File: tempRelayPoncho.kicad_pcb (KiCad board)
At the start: 2 copper layers, 36 parts, among them J1 Screw_Terminal_1x02, J2 Screw_Terminal_1x02, J3 Screw_Terminal_1x02, J4 Screw_Terminal_1x02, J5 Screw_Terminal_1x02, J6 Screw_Terminal_1x02, Q1 MMBT3904, Q2 MMBT3904, U1 NUP2105LT1G, U2 MAX31855KASA+, U3 MCP601R, U4 G5LE-1A-5DC, U6 G5LE-1A-5DC

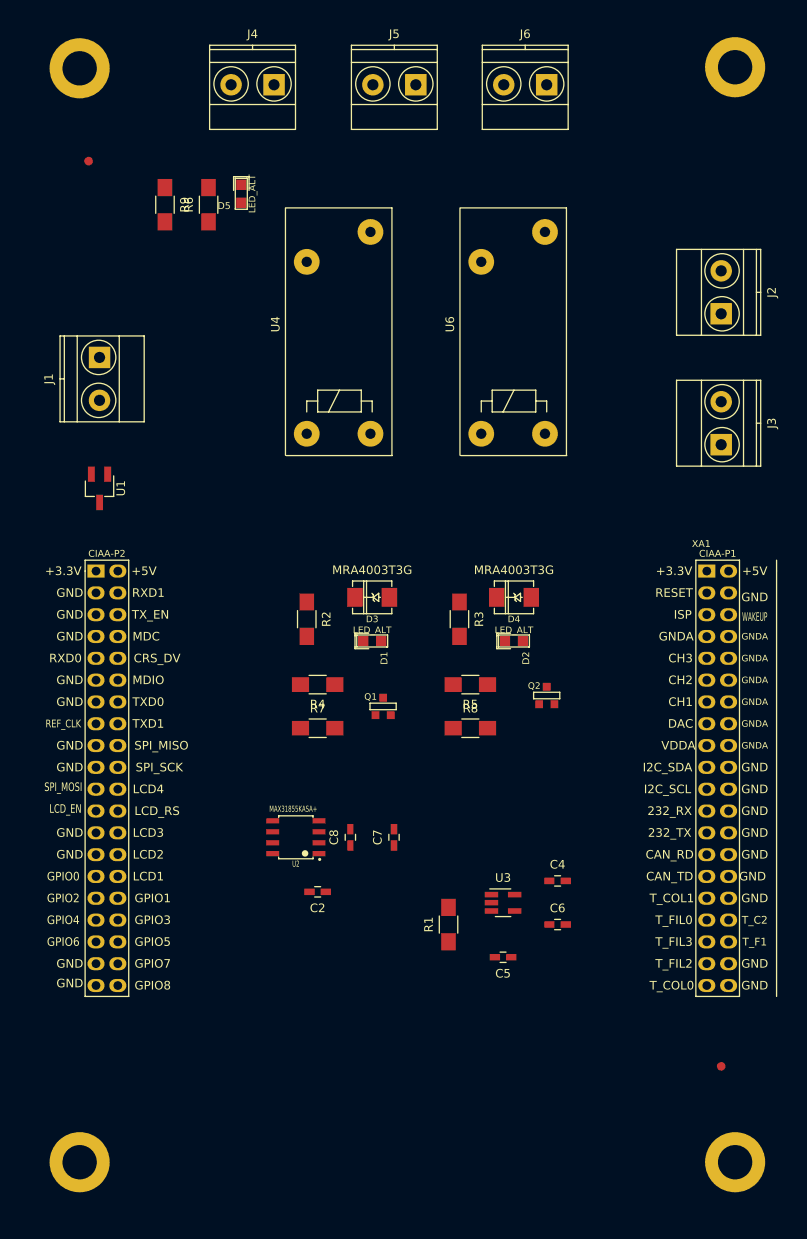
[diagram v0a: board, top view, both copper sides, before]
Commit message: Primer version del PCB
Se agregan modificaciones segun primer correccion. Se carga primer version  del PCB.
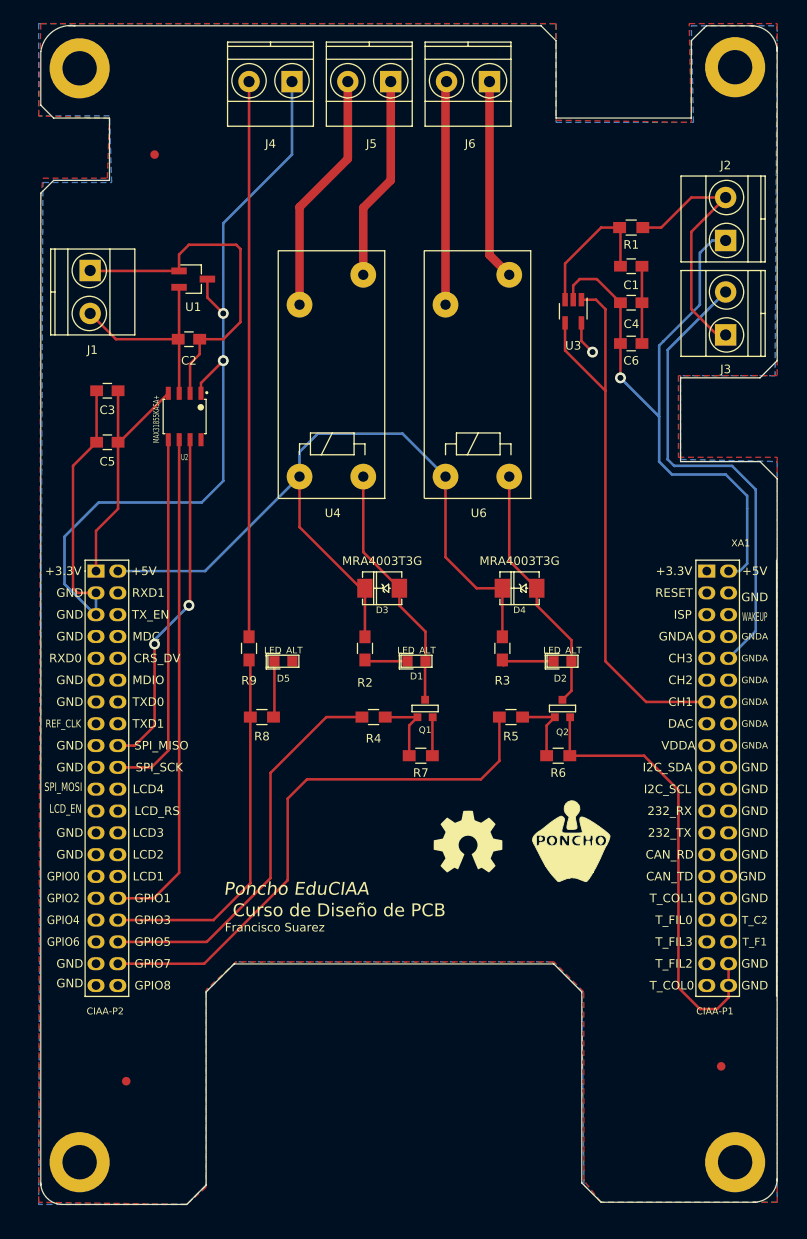
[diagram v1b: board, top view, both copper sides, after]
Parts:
- removed C7: 10u, footprints:C_0603_HandSoldering
- removed C8: 100n, footprints:C_0603_HandSoldering
- added C1: 10u, footprints:C_0805_HandSoldering, F.Cu at (147.0, 60.5)
- added C3: 10u, footprints:C_0805_HandSoldering, F.Cu at (86.0, 75.0)
- added F3: FIDUCIAL, footprints:Fiducial_1mm, F.Cu at (88.2, 155.4)
- added G***: LOGO, footprints:Logo_Poncho, F.Cu at (140.0, 127.5)
- added G101: Logo_OSHWA, footprints:Logo_OSHWA, F.Cu at (128.0, 127.5)
- C2, C4, C6: footprint footprints:C_0603_HandSoldering -> footprints:C_0805_HandSoldering
- C5: value 10u -> 100n; footprint footprints:C_0603_HandSoldering -> footprints:C_0805_HandSoldering
- R1, R2, R3, R4, R5, R7, R9: footprint footprints:R_1206_HandSoldering -> footprints:R_0805_HandSoldering
- R6: value 1k -> 10k; footprint footprints:R_1206_HandSoldering -> footprints:R_0805_HandSoldering
- R8: value 10k -> 1k; footprint footprints:R_1206_HandSoldering -> footprints:R_0805_HandSoldering
- moved R1 83.9 mm to (147.0, 56.0), turned to 0 degrees
- moved R6 76.0 mm to (138.5, 117.5), turned to 180 degrees
- moved C5 75.6 mm to (86.0, 81.0), turned to 0 degrees
- moved U3 69.4 mm to (140.2, 65.8), turned to 270 degrees
- moved C6 68.2 mm to (147.0, 69.5), turned to 180 degrees
- moved C4 67.9 mm to (147.0, 64.8), turned to 180 degrees
- moved C2 66.1 mm to (95.5, 69.0), turned to 0 degrees
- moved D5 54.7 mm to (106.5, 106.5), turned to 180 degrees
- moved R9 52.6 mm to (102.5, 105.0)
- moved U2 50.7 mm to (95.0, 78.0), turned to 270 degrees
- moved U1 26.7 mm to (96.0, 62.0), turned to 0 degrees
- moved R8 24.3 mm to (104.0, 113.0), turned to 180 degrees
- moved J3 12.8 mm to (158.0, 68.5)
- moved R7 12.4 mm to (122.5, 117.5), turned to 180 degrees
- moved J1 10.2 mm to (84.0, 61.0)
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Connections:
- net /conector_ciaa/GNDA renamed GNDA
- C5 pad 2: Net-(C5-Pad2) -> +3V3
- D3 pad 2: +5V -> +5VD
- D4 pad 2: +5V -> +5VD
- R1 pad 1: Net-(C5-Pad2) -> Net-(C1-Pad2)
- R2 pad 1: +5V -> Net-(D1-Pad2)
- R2 pad 2: Net-(D1-Pad2) -> +5VD
- R3 pad 1: +5V -> Net-(D2-Pad2)
- R3 pad 2: Net-(D2-Pad2) -> +5VD
- R4 pad 2: /conector_ciaa/GPIO_2 -> /conector_ciaa/GPIO_5
- R5 pad 2: /conector_ciaa/GPIO_3 -> /conector_ciaa/GPIO_7
- R6 pad 1: /conector_ciaa/GPIO_1 -> GND
- R6 pad 2: Net-(D5-Pad2) -> Net-(Q2-Pad1)
- R8 pad 1: GND -> Net-(D5-Pad2)
- R8 pad 2: Net-(Q2-Pad1) -> /conector_ciaa/GPIO_3
- R9 pad 2: /conector_ciaa/GPIO_1 -> /conector_ciaa/GPIO_3
- U2 pad 4: +3.3V -> +3V3
- U2 pad 6: /conector_ciaa/GPIO_0 -> /conector_ciaa/GPIO_1
- U3 pad 3: Net-(C5-Pad2) -> Net-(C1-Pad2)
- U4 pad 5: +5V -> +5VD
- U6 pad 5: +5V -> +5VD
- XA1 pad 1: +3.3V -> Net-(XA1-Pad1)
- XA1 pad 20: GND -> Net-(XA1-Pad20)
- XA1 pad 22: GND -> Net-(XA1-Pad22)
- XA1 pad 24: GND -> Net-(XA1-Pad24)
- XA1 pad 26: GND -> Net-(XA1-Pad26)
- XA1 pad 28: GND -> Net-(XA1-Pad28)
- XA1 pad 30: GND -> Net-(XA1-Pad30)
- XA1 pad 32: GND -> Net-(XA1-Pad32)
- XA1 pad 41: Net-(XA1-Pad41) -> +3V3
- XA1 pad 42: Net-(XA1-Pad42) -> +5VD
- XA1 pad 47: GND -> Net-(XA1-Pad47)
- XA1 pad 51: GND -> Net-(XA1-Pad51)
- XA1 pad 53: GND -> Net-(XA1-Pad53)
- XA1 pad 57: GND -> Net-(XA1-Pad57)
- XA1 pad 59: GND -> Net-(XA1-Pad59)
- XA1 pad 65: GND -> Net-(XA1-Pad65)
- XA1 pad 67: GND -> Net-(XA1-Pad67)
- XA1 pad 69: /conector_ciaa/GPIO_0 -> Net-(XA1-Pad69)
- XA1 pad 71: /conector_ciaa/GPIO_2 -> Net-(XA1-Pad71)
- XA1 pad 76: Net-(XA1-Pad76) -> /conector_ciaa/GPIO_5
- XA1 pad 77: GND -> Net-(XA1-Pad77)
- XA1 pad 78: Net-(XA1-Pad78) -> /conector_ciaa/GPIO_7
- XA1 pad 79: GND -> Net-(XA1-Pad79)
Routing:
- net GND: track 0.00 -> 193.0 mm, vias 0 -> 3
- net +5VD: track 0.00 -> 94.6 mm
- net +5V: track 0.00 -> 76.1 mm, vias 0 -> 1
- net /conector_ciaa/ADC_1: track 0.00 -> 67.9 mm
- net Net-(J4-Pad2): track 0.00 -> 65.4 mm
- net /conector_ciaa/GPIO_7: track 0.00 -> 64.9 mm
- net /conector_ciaa/GPIO_1: track 0.00 -> 58.9 mm
- net GNDA: track 0.00 -> 55.3 mm
- net /conector_ciaa/GPIO_5: track 0.00 -> 46.4 mm
- net /conector_ciaa/GPIO_3: track 0.00 -> 43.3 mm
- net /inputs_temp/SCK_TCUP: track 0.00 -> 42.9 mm
- net Net-(C2-Pad2): track 0.00 -> 41.0 mm
- net /inputs_temp/MISO_TCUP: track 0.00 -> 40.5 mm, vias 0 -> 2
- net +3V3: track 0.00 -> 31.4 mm
- net Net-(J2-Pad2): track 0.00 -> 31.0 mm
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- added copper zone on B.Cu, net GND
- added copper zone on F.Cu, net GND
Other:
- board outline added: 85.8 x 137.3 mm
- net class Default: trace_width 0.25 -> 0.3; via_dia 0.6 -> 1.27; via_drill 0.4 -> 0.7
- rule trace_min: 0.2 -> 0.3
- rule via_min_drill: 0.3 -> 0.7
- rule via_min_size: 0.4 -> 1.2
- board text added: "Curso de Diseño de PCB"
- board text added: "Francisco Suarez"
- board text added: "Poncho EduCIAA"

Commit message: Correcciones de Revisor
Se agregan algunas de las correcciones del revisor. Las que restan se implementaran luego.
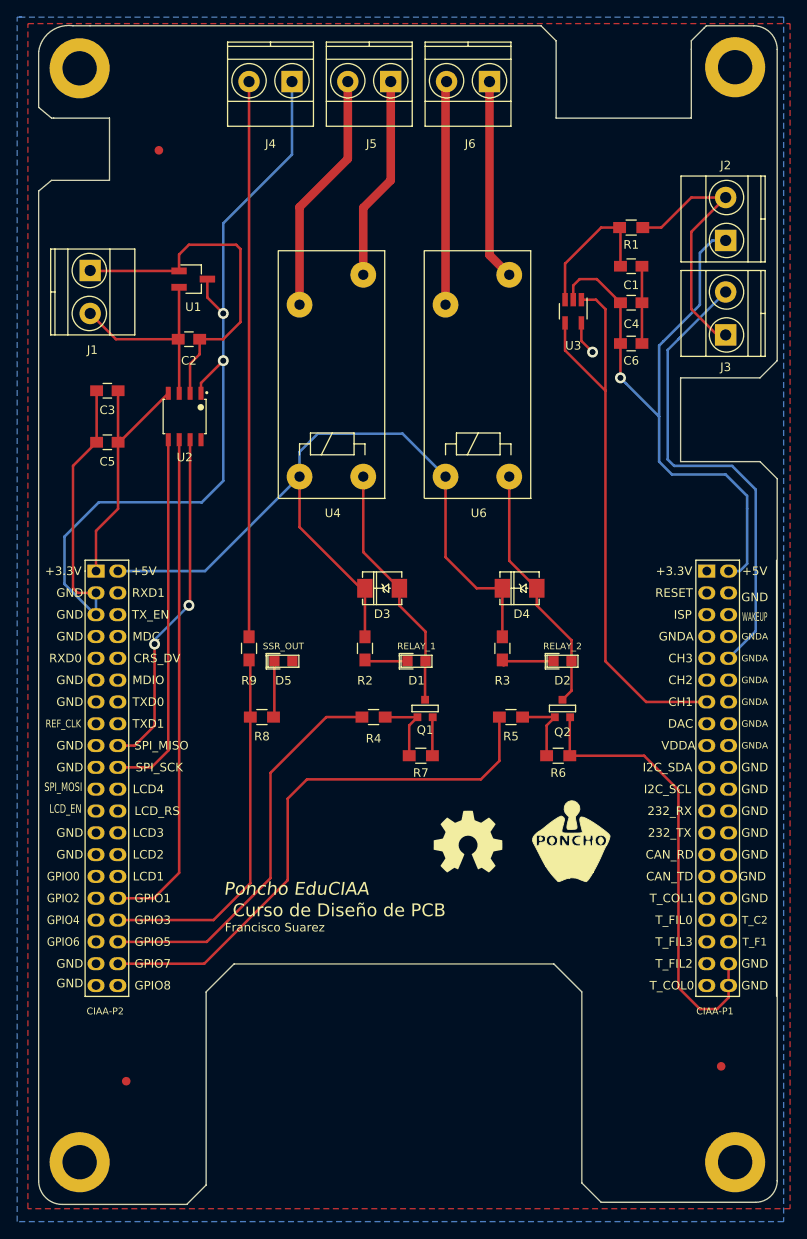
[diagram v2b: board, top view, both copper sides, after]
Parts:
- D1: value LED_ALT -> RELAY_1
- D2: value LED_ALT -> RELAY_2
- D5: value LED_ALT -> SSR_OUT
- moved F1 0.71 mm to (92.0, 47.0)
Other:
- board size 85.8 x 137.3 mm -> 86 x 137.3 mm
- board text added: "Grilla posicionamiento: 1.0 mm Grilla ruteo: 0.25 mm Pista minimo: 0.30 mm Vía minimo: 1.27 mm Agujero minimo: 0.70 mm Capas: 2 Terminación superficial: HSAL"
- board text added: "STACK-UP"

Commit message: Correccion Final
Se trabajo sobre correcciones de 2da revision. Se agregaron archivos gerbers, BOM, y objetos 3D
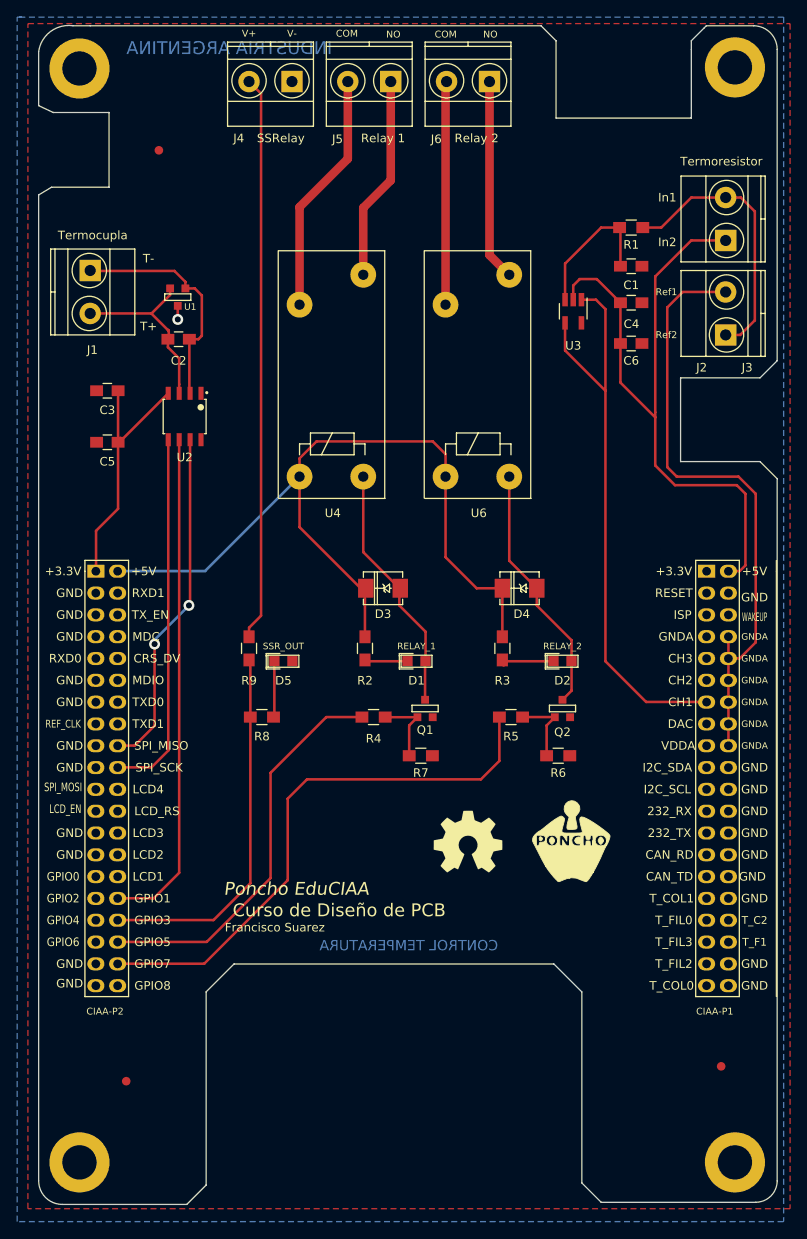
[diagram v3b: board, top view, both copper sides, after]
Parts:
- U1: footprint footprints:SC-59_Handsoldering -> footprints:SOT23_NPN
- moved U1 2.77 mm to (94.2, 64.1)
- moved C2 1.20 mm to (94.3, 69.0)
- moved D3 0.10 mm to (118.1, 98.0)
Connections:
- XA1 pad 12: Net-(XA1-Pad12) -> GNDA
- XA1 pad 14: Net-(XA1-Pad14) -> GNDA
- XA1 pad 16: Net-(XA1-Pad16) -> GNDA
- XA1 pad 18: Net-(XA1-Pad18) -> GNDA
- XA1 pad 20: Net-(XA1-Pad20) -> GND
- XA1 pad 22: Net-(XA1-Pad22) -> GND
- XA1 pad 24: Net-(XA1-Pad24) -> GND
- XA1 pad 26: Net-(XA1-Pad26) -> GND
- XA1 pad 28: Net-(XA1-Pad28) -> GND
- XA1 pad 30: Net-(XA1-Pad30) -> GND
- XA1 pad 32: Net-(XA1-Pad32) -> GND
- XA1 pad 47: Net-(XA1-Pad47) -> GND
- XA1 pad 51: Net-(XA1-Pad51) -> GND
- XA1 pad 53: Net-(XA1-Pad53) -> GND
- XA1 pad 57: Net-(XA1-Pad57) -> GND
- XA1 pad 59: Net-(XA1-Pad59) -> GND
- XA1 pad 65: Net-(XA1-Pad65) -> GND
- XA1 pad 67: Net-(XA1-Pad67) -> GND
- XA1 pad 77: Net-(XA1-Pad77) -> GND
- XA1 pad 79: Net-(XA1-Pad79) -> GND
- XA1 pad 8: Net-(XA1-Pad8) -> GNDA
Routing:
- net GND: track 193.0 -> 2.63 mm, vias 3 -> 1
- net GNDA: track 55.3 -> 71.7 mm
- net Net-(C2-Pad2): track 41.0 -> 27.4 mm
- net +5V: track 76.1 -> 78.5 mm, vias 1 -> 0
- net Net-(J2-Pad2): track 31.0 -> 32.9 mm
- net Net-(C2-Pad1): track 24.2 -> 22.2 mm
- net Net-(J4-Pad2): track 65.4 -> 66.5 mm
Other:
- outline, holes or cut-outs redrawn
- board text added: "COM"
- board text added: "CONTROL TEMPERATURA"
- board text added: "Grilla posicionamiento: 1.0 mm Grilla ruteo: 0.25 mm Pista minimo: 0.30 mm Vía minimo: 1.27 mm Margen: 0.20 mm Agujero minimo: 0.70 mm Capas: 2 Terminación superficial: HSAL"
- board text added: "INDUSTRIA ARGENTINA"
- board text added: "In1"
- board text added: "In2"
- board text added: "NO"
- board text added: "Ref1"
- board text added: "Ref2"
- board text added: "Relay 1"
- board text added: "Relay 2"
- board text added: "SSRelay"
- board text added: "T+"
- board text added: "T-"
- board text added: "Termocupla"
- board text added: "Termoresistor"
- board text added: "V+"
- board text added: "V-"
- board text removed: "Grilla posicionamiento: 1.0 mm Grilla ruteo: 0.25 mm Pista minimo: 0.30 mm Vía minimo: 1.27 mm Agujero minimo: 0.70 mm Capas: 2 Terminación superficial: HSAL"
